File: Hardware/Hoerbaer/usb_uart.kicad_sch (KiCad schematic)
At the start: 17 parts, among them J11 USB2_UART, Q5 S8050, Q6 S8050, U11 CH343P

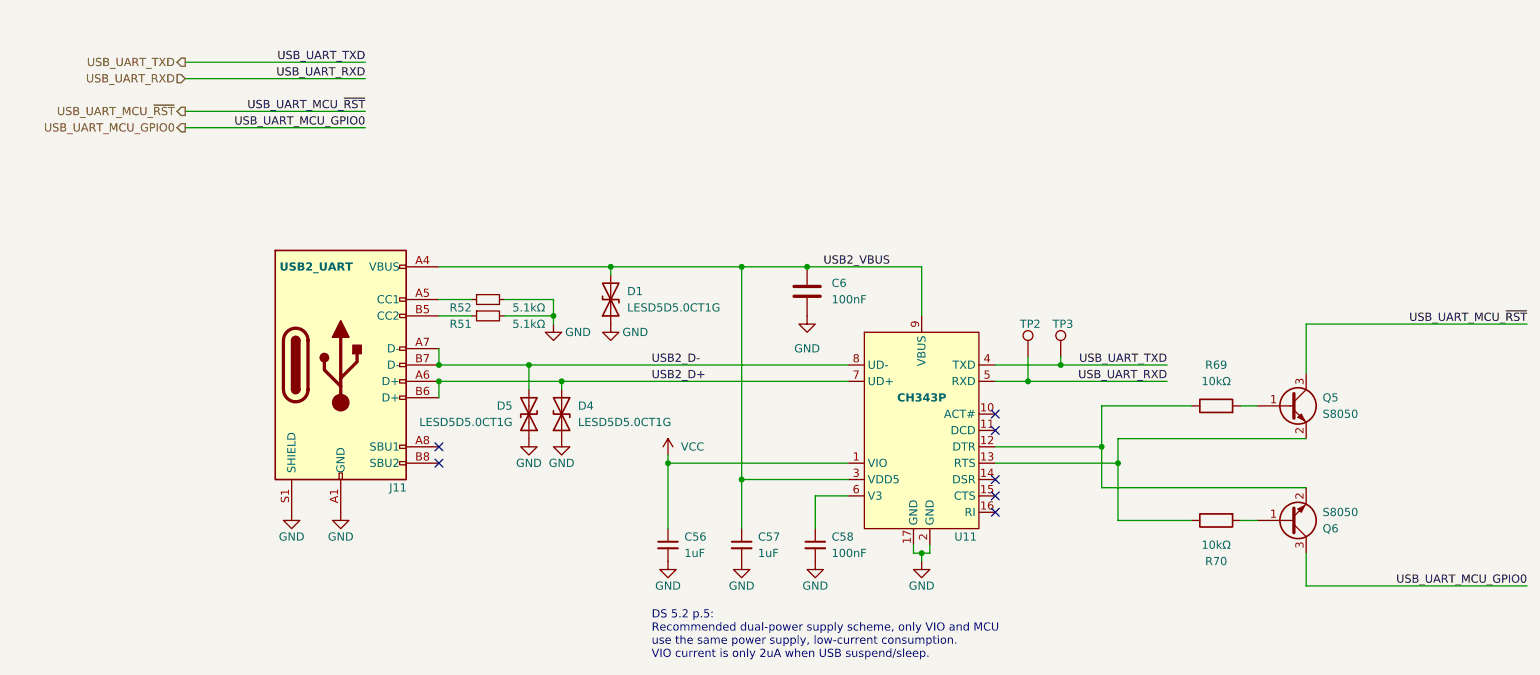
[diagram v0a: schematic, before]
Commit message: Added an additional connector. And silk screen designs.
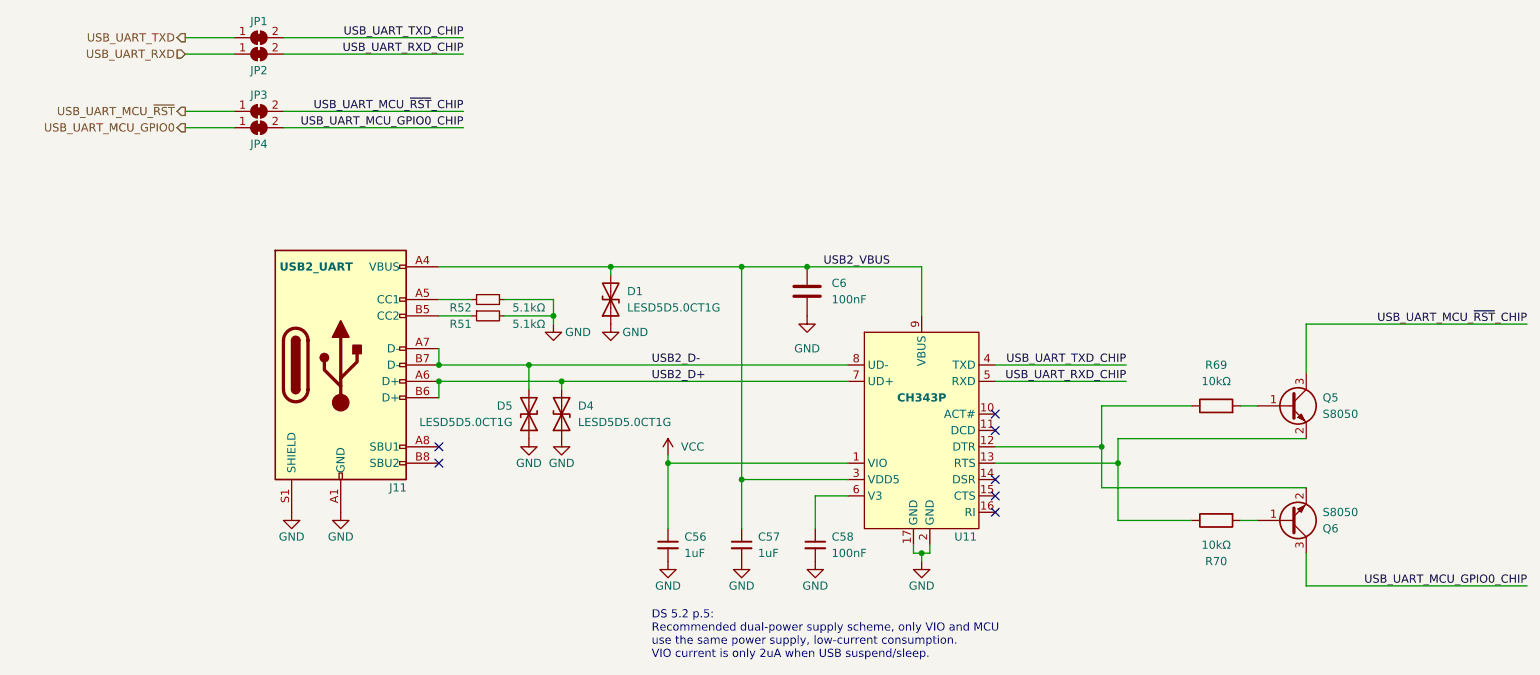
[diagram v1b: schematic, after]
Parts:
- removed TP2: CH343_RXD, TestPoint:TestPoint_Pad_D1.5mm, symbol Connector:TestPoint
- removed TP3: CH343_TXD, TestPoint:TestPoint_Pad_D1.5mm, symbol Connector:TestPoint
- added JP1: CH_TX, Jumper:SolderJumper-2_P1.3mm_Bridged_RoundedPad1.0x1.5mm, symbol Jumper:SolderJumper_2_Bridged
- added JP2: CH_RX, Jumper:SolderJumper-2_P1.3mm_Bridged_RoundedPad1.0x1.5mm, symbol Jumper:SolderJumper_2_Bridged
- added JP3: ~{RST}, Jumper:SolderJumper-2_P1.3mm_Bridged_RoundedPad1.0x1.5mm, symbol Jumper:SolderJumper_2_Bridged
- added JP4: IO0, Jumper:SolderJumper-2_P1.3mm_Bridged_RoundedPad1.0x1.5mm, symbol Jumper:SolderJumper_2_Bridged
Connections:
- net USB_UART_MCU_GPIO0: now also JP4.1 (A); no longer Q6.3 (C)
- net USB_UART_MCU_~{RST}: now also JP3.1 (A); no longer Q5.3 (C)
- net USB_UART_RXD: now also JP2.1 (A); no longer U11.5 (RXD)
- net USB_UART_TXD: now also JP1.1 (A); no longer U11.4 (TXD)
- new net USB_UART_MCU_GPIO0_CHIP: JP4.2 (B), Q6.3 (C)
- new net USB_UART_MCU_~{RST}_CHIP: JP3.2 (B), Q5.3 (C)
- new net USB_UART_RXD_CHIP: JP2.2 (B), U11.5 (RXD)
- new net USB_UART_TXD_CHIP: JP1.2 (B), U11.4 (TXD)

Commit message: Fixed 1uF order number.
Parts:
- C56, C57: LCSC C726581 -> C29266; MPN AC0805KKX7R6BB105 -> CL05A105KO5NNNC
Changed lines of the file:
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@@
       (effects (font (size 1.27 1.27)) hide)
     )
-    (property "LCSC" "C726581" (at 114.3 107.95 0)
+    (property "LCSC" "C29266 " (at 114.3 107.95 0)
       (effects (font (size 1.27 1.27)) hide)
     )
-    (property "MPN" "AC0805KKX7R6BB105" (at 114.3 107.95 0)
+    (property "MPN" "CL05A105KO5NNNC" (at 114.3 107.95 0)
       (effects (font (size 1.27 1.27)) hide)
     )
@@
       (effects (font (size 1.27 1.27)) hide)
     )
-    (property "LCSC" "C726581" (at 125.73 107.95 0)
+    (property "LCSC" "C29266 " (at 125.73 107.95 0)
       (effects (font (size 1.27 1.27)) hide)
     )
-    (property "MPN" "AC0805KKX7R6BB105" (at 125.73 107.95 0)
+    (property "MPN" "CL05A105KO5NNNC" (at 125.73 107.95 0)
       (effects (font (size 1.27 1.27)) hide)
     )

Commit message: Added 3d model for USB footprint.
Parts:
- J11: footprint Connector_USB:USB_C_Receptacle_HRO_TYPE-C-31-M-12 -> Baer_Footprints:USB_C_Receptacle_HRO_TYPE-C-31-M-12
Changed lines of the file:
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@@
       (effects (font (size 1.27 1.27) bold))
     )
-    (property "Footprint" "Connector_USB:USB_C_Receptacle_HRO_TYPE-C-31-M-12" (at 67.31 80.01 0)
+    (property "Footprint" "Baer_Footprints:USB_C_Receptacle_HRO_TYPE-C-31-M-12" (at 67.31 80.01 0)
       (effects (font (size 1.27 1.27)) hide)
     )

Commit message: WIP new hw rev
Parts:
- renumbered C56 to C63, C57 to C64, C6 to C65, C58 to C66, D1 to D10, D5 to D8, D4 to D9, J11 to J18, JP1 to JP6, JP2 to JP7, JP3 to JP8, JP4 to JP9, Q5 to Q1, Q6 to Q2, R52 to R64, R51 to R65, R69 to R66, R70 to R67, U11 to U13
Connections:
- net USB2_VBUS renamed VBUS_USB2
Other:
- moved on the sheet: C65

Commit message: BOM FIxes
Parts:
- C65, C66: LCSC C458949 -> C1525; MPN MT15B104K160CT -> CL05B104KO5NNNC
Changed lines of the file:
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@@
 			)
 		)
-		(property "LCSC" "C458949"
-			(at 168.91 63.5 0)
-			(effects
-				(font
-					(size 1.27 1.27)
-				)
-				(hide yes)
-			)
-		)
-		(property "MPN" "MT15B104K160CT"
+		(property "LCSC" "C1525"
+			(at 168.91 63.5 0)
+			(effects
+				(font
+					(size 1.27 1.27)
+				)
+				(hide yes)
+			)
+		)
+		(property "MPN" "CL05B104KO5NNNC"
 			(at 168.91 63.5 0)
 			(effects
@@
 			)
 		)
-		(property "LCSC" "C458949"
+		(property "LCSC" "C1525"
 			(at 137.16 107.95 0)
 			(effects
@@
 			)
 		)
-		(property "MPN" "MT15B104K160CT"
+		(property "MPN" "CL05B104KO5NNNC"
 			(at 137.16 107.95 0)
 			(effects

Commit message: Production
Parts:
- J18: FT Position Offset (none) -> 0.0,1.35; JLCPCB Position Offset 0.0,1.35 -> (none)
- Q1, Q2: JLCPCB Rotation Offset 180 -> (none)
- U13: FT Rotation Offset (none) -> 180
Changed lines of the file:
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@@
-			)
-		)
-		(property "JLCPCB Rotation Offset" "180"
-			(at 210.82 86.36 0)
-			(effects
-				(font
-					(size 1.27 1.27)
-				)
-				(hide yes)
 			)
 		)
@@
 		)
 		(property "SnapEDA_Link" ""
+			(at 210.82 86.36 0)
+			(effects
+				(font
+					(size 1.27 1.27)
+				)
+			)
+		)
+		(property "FT Rotation Offset" ""
 			(at 210.82 86.36 0)
 			(effects
@@
 			)
 		)
-		(property "JLCPCB Position Offset" "0.0,1.35"
-			(at 63.5 80.01 0)
-			(effects
-				(font
-					(size 1.27 1.27)
-				)
-				(hide yes)
-			)
-		)
 		(property "Check_prices" ""
 			(at 63.5 80.01 0)
@@
 		)
 		(property "SnapEDA_Link" ""
+			(at 63.5 80.01 0)
+			(effects
+				(font
+					(size 1.27 1.27)
+				)
+			)
+		)
+		(property "FT Position Offset" "0.0,1.35"
 			(at 63.5 80.01 0)
 			(effects
@@
 			)
 		)
-		(property "JLCPCB Rotation Offset" "180"
-			(at 210.82 104.14 0)
-			(effects
-				(font
-					(size 1.27 1.27)
-				)
-				(hide yes)
-			)
-		)
 		(property "Check_prices" ""
 			(at 210.82 104.14 0)
@@
 		)
 		(property "SnapEDA_Link" ""
+			(at 210.82 104.14 0)
+			(effects
+				(font
+					(size 1.27 1.27)
+				)
+			)
+		)
+		(property "FT Rotation Offset" ""
 			(at 210.82 104.14 0)
 			(effects
@@
 			(at 153.67 92.71 0)
 			(effects
+				(font
+					(size 1.27 1.27)
+				)
+			)
+		)
+		(property "FT Rotation Offset" "180"
+			(at 153.67 92.71 0)
+			(effects
